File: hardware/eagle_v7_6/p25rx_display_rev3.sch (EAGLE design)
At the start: 79 parts, among them J1 SJ-3523, J2 USB4085, J3 1050170001, J4 SJ-3523, J5 SF: PRT-10361, J7 SF: PRT-10361, Q1 IRFR5305, Q16 2N7002, SW2 CHS-01TA, U1 LCD24, U10 AT25F512ASOIC, U2 IS31AP4991A-GRLS2-TR, U4 STM32H743ZIT6, U5 CS4344, U6 MCP1826ST-3302E/DB, X2 8MHZ

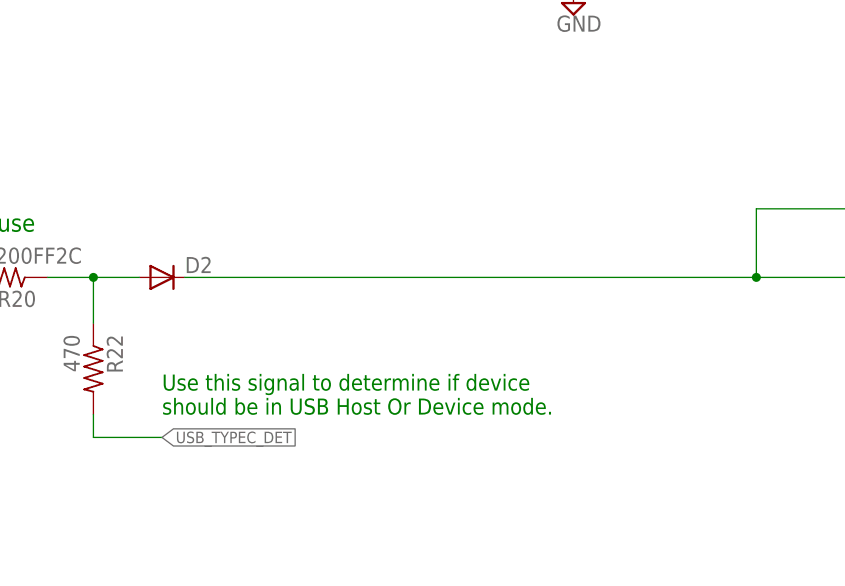
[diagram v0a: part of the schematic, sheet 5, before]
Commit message: update notes on schematic regarding D2
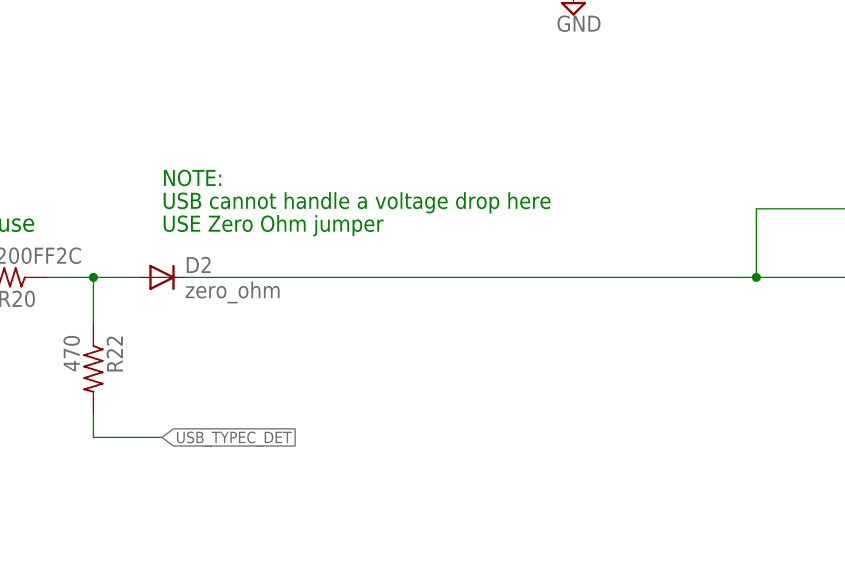
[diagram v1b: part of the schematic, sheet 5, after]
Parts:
- D2: value (none) -> zero_ohm
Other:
- note added: "2021-04-21 - add notes regarding D2 being replaced with zero ohm jumper"
- note added: "NOTE:"
- note added: "USB cannot handle a voltage drop here"
- note added: "USE Zero Ohm jumper"
- note removed: "Use this signal to determine if device should be in USB Host Or Device mode."
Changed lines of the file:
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@@
 <part name="R6" library="misc9" deviceset="R-US_" device="R0402" value="4.99k"/>
 <part name="J3" library="usb-dvi-hdmi-connectors" deviceset="1050170001" device=""/>
-<part name="D2" library="diode" deviceset="DIODE-" device="SMB"/>
+<part name="D2" library="diode" deviceset="DIODE-" device="SMB" value="zero_ohm"/>
 <part name="Q16" library="fets" deviceset="2N7002" device="" value="2N7002"/>
 <part name="SUPPLY372" library="supply2" deviceset="GND" device=""/>
@@
 <text x="139.7" y="76.2" size="1.9304" layer="91">USB Micro AB OTG Connector</text>
 <text x="147.32" y="71.12" size="1.9304" layer="91">Power + Data</text>
-<text x="101.6" y="-7.62" size="1.778" layer="91">Use this signal to determine if device
-should be in USB Host Or Device mode.</text>
+<text x="101.6" y="15.24" size="1.778" layer="91">USB cannot handle a voltage drop here</text>
+<text x="101.6" y="12.7" size="1.778" layer="91">USE Zero Ohm jumper</text>
+<text x="101.6" y="17.78" size="1.778" layer="91">NOTE:</text>
 </plain>
 <instances>
@@
 <text x="20.32" y="83.82" size="1.778" layer="91">changes: rev2b-&gt;rev3</text>
 <frame x1="10.16" y1="-17.78" x2="190.5" y2="91.44" columns="8" rows="5" layer="91"/>
-<text x="22.86" y="73.66" size="1.778" layer="91">Speaker jack changed to mono-only (connect to right side)</text>
+<text x="20.32" y="81.28" size="1.778" layer="91">Speaker jack changed to mono-only (connect to right side)</text>
+<text x="20.32" y="71.12" size="1.778" layer="91">2021-04-21 - add notes regarding D2 being replaced with zero ohm jumper</text>
 </plain>
 <instances>
